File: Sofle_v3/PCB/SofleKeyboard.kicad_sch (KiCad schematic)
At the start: 97 parts, among them SW1 SW_PUSH-MX_W_LED

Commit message: design: routing and schematic beatifications
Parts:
- D1, D10, D11, D12, D13, D14, D15, D16, D17, D18, D19, D2, D20, D21, D22, D23, D24, D25, D26, D27, D28, D29, D3, D30, D4, D5, D6, D7, D8, D9: value (none) -> D; footprint (none) -> Diode_SMD:crkbd-diode
- D31, D32, D33, D34, D35, D36, D37: value (none) -> LED_sk2812_SM; footprint LED_SMD:LED_WS2812B_PLCC4_5.0x5.0mm_P3.2mm -> SofleRGB:LED_WS2812B_TwoSided; symbol SofleKeyboard:LED_sk2812_SM -> SofleKeyboard:LED_ws2812_SM
- J1: value (none) -> LED; footprint (none) -> SofleKeyboard-footprint:LED
- J2: value (none) -> 4PIN; footprint (none) -> SofleRGB:WM2211210044
- J3: value (none) -> OLED; footprint (none) -> SofleKeyboard-footprint:OLED_4Pin
- J4: value (none) -> key leds; footprint (none) -> Connector:3x1header
- J5: value (none) -> backlight sel; footprint (none) -> Connector:3x1header
- J6: value (none) -> indicator bypass; footprint (none) -> Connector:3x1header
- JP1, JP2, JP3, JP4, JP5, JP6, JP7, JP8: value (none) -> Jumper_NO_Small; footprint (none) -> SofleKeyboard-footprint:Jumper
- P1, P2: value (none) -> i2c_pin; footprint (none) -> SofleKeyboard-footprint:1pin_conn
- R1, R2: value (none) -> R; footprint (none) -> SofleKeyboard-footprint:RESISTOR_mini
- RSW1: value (none) -> SW_RST; footprint (none) -> SofleRGB:TPS635-1B43D
- SW10, SW11, SW12, SW13, SW14, SW15, SW16, SW17, SW18, SW19, SW2, SW20, SW21, SW22, SW23, SW24, SW26, SW27, SW28, SW29, SW3, SW30, SW4, SW5, SW6, SW7, SW8, SW9: value (none) -> SW_PUSH-MX_W_LED
- SW25: value (none) -> Rotary_Encoder_Switch; footprint (none) -> SofleKeyboard-footprint:RotaryEncoder_Alps_EC11E-Switch_Vertical_H20mm-keebio_modified
- U1: value (none) -> ProMicro; footprint (none) -> SofleKeyboard-footprint:ProMicro
- W1: value (none) -> jumper; footprint (none) -> SofleKeyboard-footprint:jumper_data
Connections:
- net GND: now also D31.3 (VSS), D32.3 (VSS), D33.3 (VSS), D34.3 (VSS), D35.3 (VSS), D36.3 (VSS), D37.4 (DIN); no longer D31.2 (VSS), D32.2 (VSS), D33.2 (VSS), D34.2 (VSS), D35.2 (VSS), D36.2 (VSS), D37.2 (VSS)
- net VCC: now also D31.1 (VDD), D32.1 (VDD), D33.1 (VDD), D34.1 (VDD), D35.1 (VDD), D36.1 (VDD), D37.2 (DOUT); no longer D31.4 (VDD), D32.4 (VDD), D33.4 (VDD), D34.4 (VDD), D35.4 (VDD), D36.4 (VDD), D37.4 (VDD)
- net backlight: now also SW30.4 (DIN); no longer SW30.2 (DIN)
- net underglow: now also D33.4 (DIN); no longer D33.3 (DIN)
- net SW26_D: now reaches D26.2 (A), SW26.5
- net SW1_D: now reaches D1.2 (A), SW1.5
- net SW2_D: now reaches D2.2 (A), SW2.5
- net SW3_D: now reaches D3.2 (A), SW3.5
- net SW4_D: now reaches D4.2 (A), SW4.5
- net SW5_D: now reaches D5.2 (A), SW5.5
- net SW6_D: now reaches D6.2 (A), SW6.5
- net SW8_D: now reaches D8.2 (A), SW8.5
- net SW9_D: now reaches D9.2 (A), SW9.5
- net SW10_D: now reaches D10.2 (A), SW10.5
- net SW11_D: now reaches D11.2 (A), SW11.5
- net SW12_D: now reaches D12.2 (A), SW12.5
- net SW7_D: now reaches D7.2 (A), SW7.5
- net SW13_D: now reaches D13.2 (A), SW13.5
- net SW14_D: now reaches D14.2 (A), SW14.5
- net SW15_D: now reaches D15.2 (A), SW15.5
- net SW16_D: now reaches D16.2 (A), SW16.5
- net SW17_D: now reaches D17.2 (A), SW17.5
- net SW18_D: now reaches D18.2 (A), SW18.5
- net SW21_D: now reaches D21.2 (A), SW21.5
- net SW22_D: now reaches D22.2 (A), SW22.5
- net SW23_D: now reaches D23.2 (A), SW23.5
- net SW24_D: now reaches D24.2 (A), SW24.5
- net SW20_D: now reaches D20.2 (A), SW20.5
- net SW19_D: now reaches D19.2 (A), SW19.5
- net SW27_D: now reaches D27.2 (A), SW27.5
- net SW28_D: now reaches D28.2 (A), SW28.5
- net SW29_D: now reaches D29.2 (A), SW29.5
- net SW30_D: now reaches D30.2 (A), SW30.5
- net at SW1.2 (DOUT): now also SW7.4 (DIN); no longer SW2.4 (DOUT)
- net at SW1.4 (DIN): now also SW2.2 (DOUT); no longer SW7.2 (DIN)
- net at SW8.4 (DIN): now also SW14.2 (DOUT); no longer SW2.2 (DIN)
- net at SW3.2 (DOUT): now also SW9.4 (DIN); no longer SW4.4 (DOUT)
- net at SW3.4 (DIN): now also SW4.2 (DOUT); no longer SW9.2 (DIN)
- net at SW10.4 (DIN): now also SW16.2 (DOUT); no longer SW4.2 (DIN)
- net at SW5.2 (DOUT): now also SW11.4 (DIN); no longer SW6.4 (DOUT)
- net at SW5.4 (DIN): now also SW6.2 (DOUT); no longer SW11.2 (DIN)
- net at SW12.4 (DIN): now also SW18.2 (DOUT); no longer SW6.2 (DIN)
- net at SW13.2 (DOUT): now also SW19.4 (DIN); no longer SW7.4 (DOUT)
- net at SW8.2 (DOUT): now also SW2.4 (DIN); no longer SW14.4 (DOUT)
- net at SW15.2 (DOUT): now also SW21.4 (DIN); no longer SW9.4 (DOUT)
- net at SW10.2 (DOUT): now also SW4.4 (DIN); no longer SW16.4 (DOUT)
- net at SW17.2 (DOUT): now also SW23.4 (DIN); no longer SW11.4 (DOUT)
- net at SW12.2 (DOUT): now also SW6.4 (DIN); no longer SW18.4 (DOUT)
- net at SW24.2 (DOUT): now also SW18.4 (DIN); no longer SW30.4 (DOUT)
- net at SW24.4 (DIN): now also SW30.2 (DOUT); no longer SW18.2 (DIN)
- net at SW17.4 (DIN): now also SW11.2 (DOUT); no longer SW23.2 (DIN)
- net at SW29.2 (DOUT): now also SW28.4 (DIN); no longer SW23.4 (DOUT)
- net at SW22.2 (DOUT): now also SW16.4 (DIN); no longer SW28.4 (DOUT)
- net at SW22.4 (DIN): now also SW28.2 (DOUT); no longer SW16.2 (DIN)
- net at SW15.4 (DIN): now also SW9.2 (DOUT); no longer SW21.2 (DIN)
- net at SW27.2 (DOUT): now also SW26.4 (DIN); no longer SW21.4 (DOUT)
- net at SW20.2 (DOUT): now also SW14.4 (DIN); no longer SW26.4 (DOUT)
- net at SW20.4 (DIN): now also SW26.2 (DOUT); no longer SW14.2 (DIN)
- net at SW13.4 (DIN): now also SW7.2 (DOUT); no longer SW19.2 (DIN)
- net at SW29.4 (DIN): now also SW23.2 (DOUT); no longer SW28.2 (DIN)
- net at SW27.4 (DIN): now also SW21.2 (DOUT); no longer SW26.2 (DIN)
- net at J5.2 (Pin_2): now also D36.2 (DOUT); no longer D36.1 (DOUT)
- net SW25A renamed col5
- new net: D31.2 (DOUT), D34.4 (DIN)
- new net: D31.4 (DIN), D32.2 (DOUT)
- new net: D32.4 (DIN), D33.2 (DOUT)
- new net: D34.2 (DOUT), D35.4 (DIN)
- new net: D35.2 (DOUT), D36.4 (DIN)
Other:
- note added: "TODO: - Underglow LED positioning (carefull with mounting holes - enough space to them) - Reset button footprint - Routing of everything :)))))))) - Encoder daughterboard Erledigt: - Headphone Jack footprint"
- note removed: "TODO: - Underglow LED positioning - Headphone Jack footprint - Reset button footprint - Routing of everything :)))))))) - Encoder daughterboard"
- moved on the sheet: D1, D10, D11, D12, D13, D14, D15, D16, D17, D18, D19, D2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

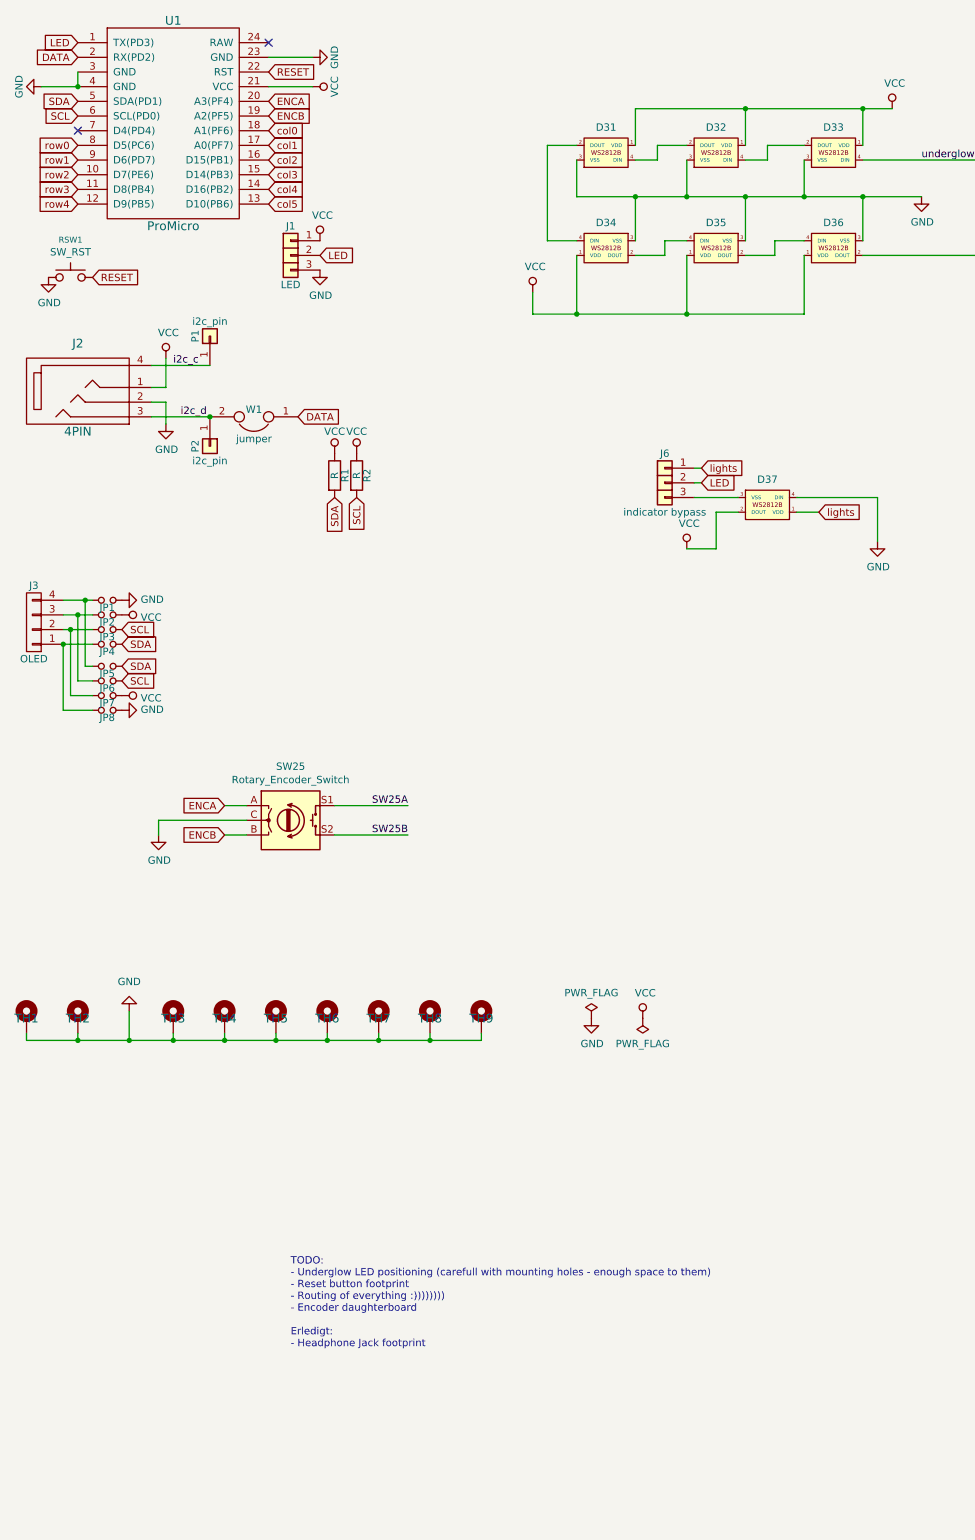
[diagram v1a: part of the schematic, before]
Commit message: design: added/changed daughterboard footprint also added jumpers for rotatry encoder side switch
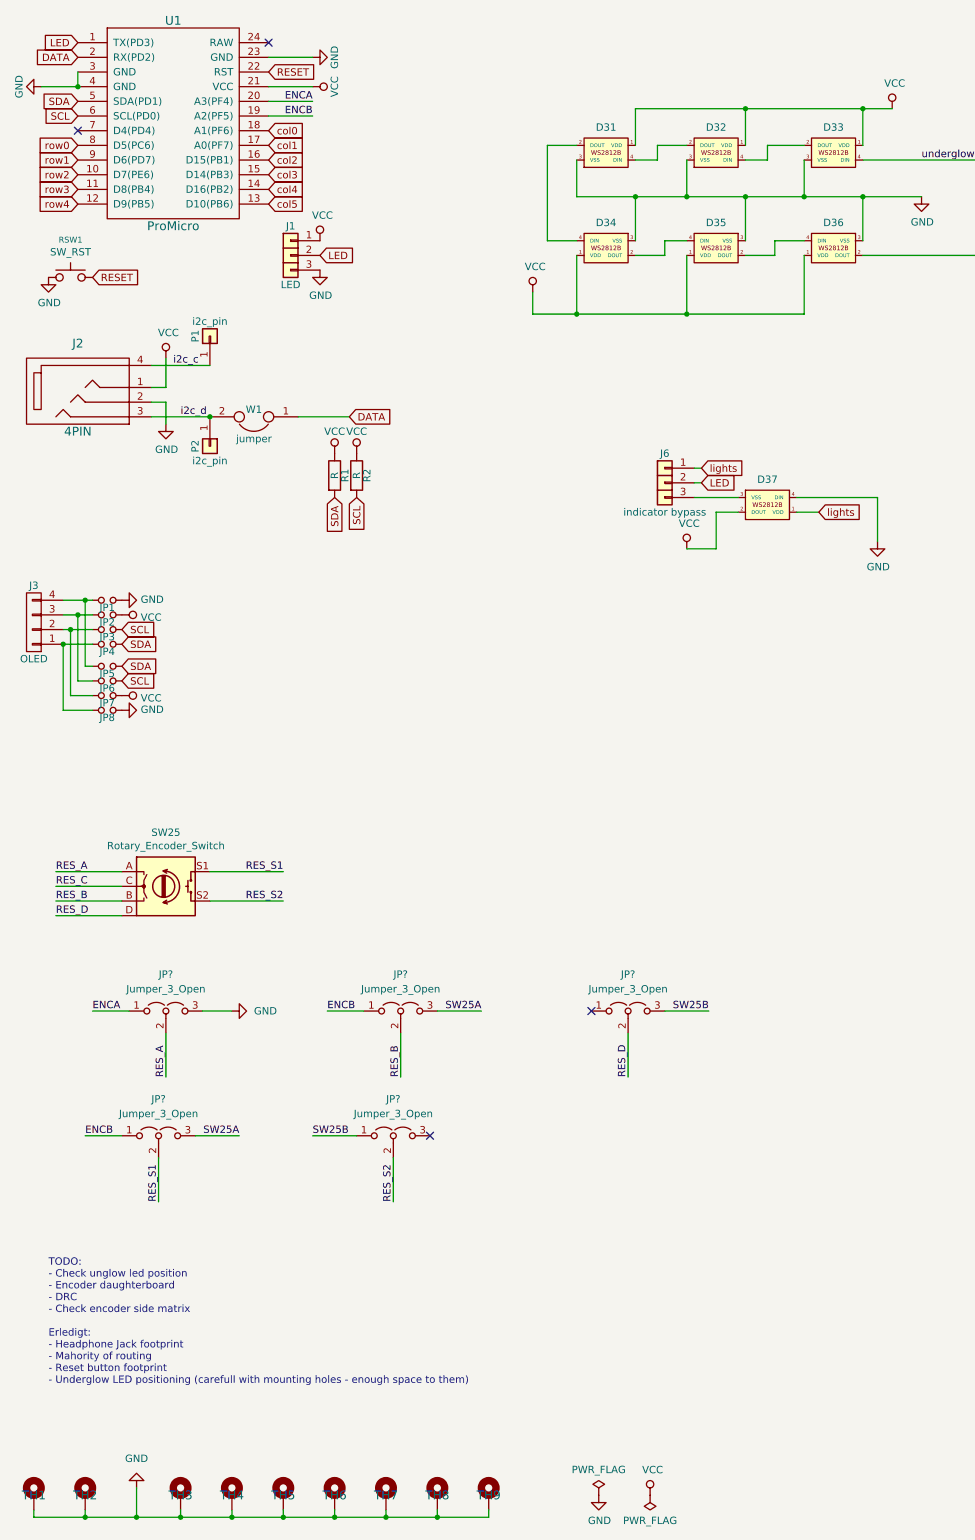
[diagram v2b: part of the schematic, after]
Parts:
- added JP? (x5): Jumper_3_Open, symbol Jumper:Jumper_3_Open
- SW25: footprint SofleKeyboard-footprint:RotaryEncoder_Alps_EC11E-Switch_Vertical_H20mm-keebio_modified -> SofleRGB:EVQWGD001_DaughterBoard; symbol SofleKeyboard-rescue:Rotary_Encoder_Switch-Device -> SofleKeyboard:RotaryEncoder_Switch4
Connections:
- net ENCA: now also JP?.1 (A); no longer SW25.A
- net ENCB: now also JP?.1 (A), JP?.1 (A); no longer SW25.B
- net GND: now also JP?.3 (B); no longer SW25.C
- net SW25B: now also JP?.1 (A), JP?.3 (B); no longer SW25.S2
- net col5: now also JP?.3 (B), JP?.3 (B); no longer SW25.S1
- new net RES_A: JP?.2 (C), SW25.A
- new net RES_B: JP?.2 (C), SW25.B
- new net RES_C: SW25.C
- new net RES_D: JP?.2 (C), SW25.D
- new net RES_S1: JP?.2 (C), SW25.S1
- new net RES_S2: JP?.2 (C), SW25.S2
- no-connect marks 4 -> 6
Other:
- note added: "TODO: - Check unglow led position - Encoder daughterboard - DRC - Check encoder side matrix Erledigt: - Headphone Jack footprint - Mahority of routing - Reset button footprint - Underglow LED positioning (carefull with mounting holes - enough space to them)"
- note removed: "TODO: - Underglow LED positioning (carefull with mounting holes - enough space to them) - Reset button footprint - Routing of everything :)))))))) - Encoder daughterboard Erledigt: - Headphone Jack footprint"
- moved on the sheet: TH1, TH2, TH3, TH4, TH5, TH6, TH7, TH8, TH9

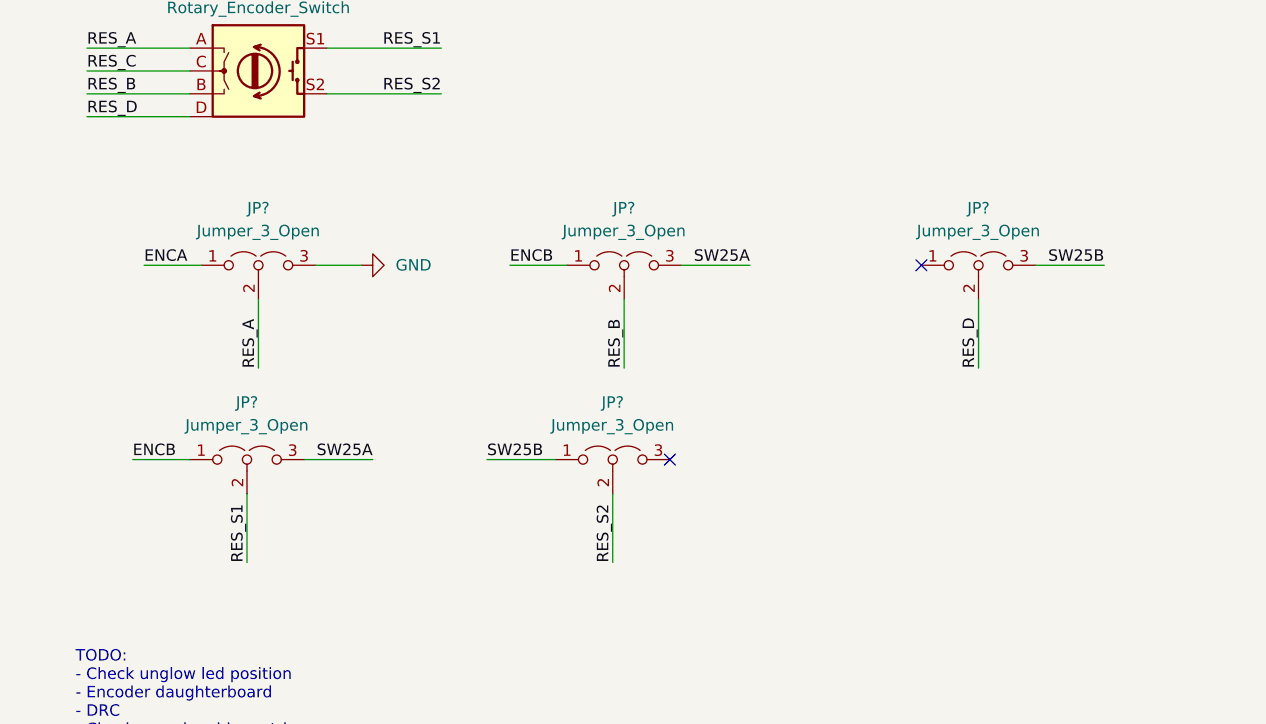
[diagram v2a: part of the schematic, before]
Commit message: design: minor orientation change added daughterboard first drc checks
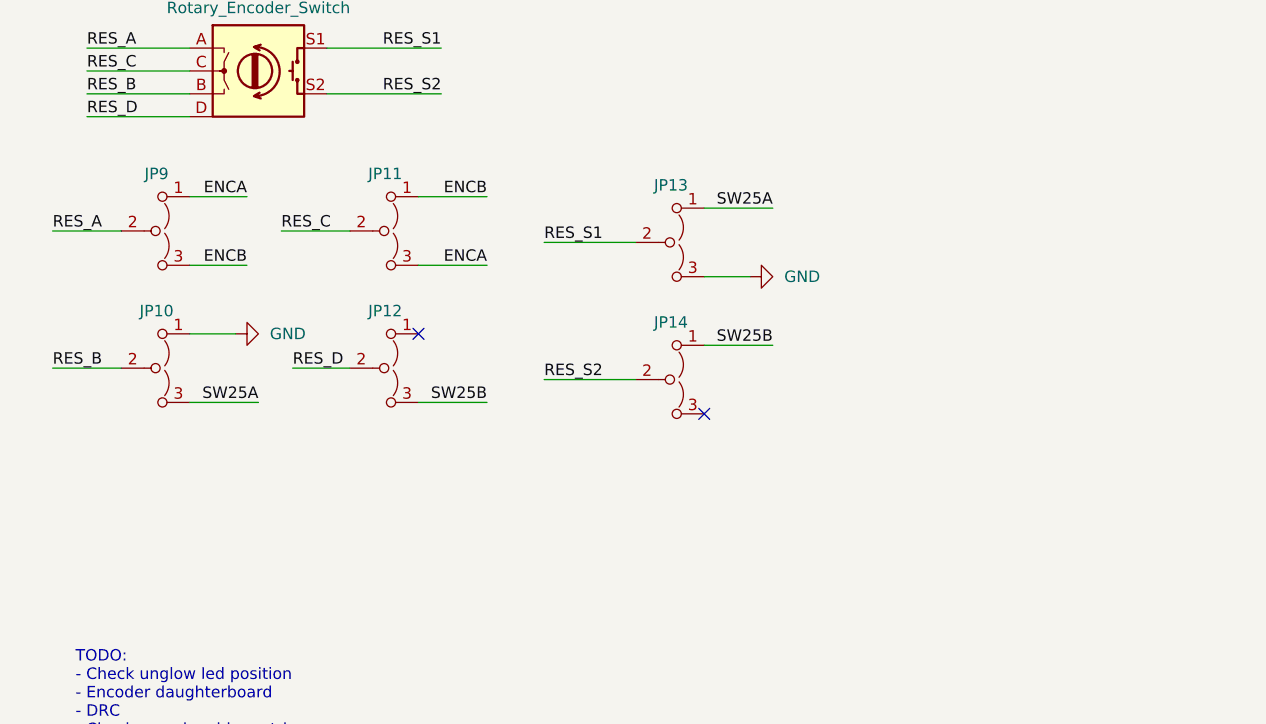
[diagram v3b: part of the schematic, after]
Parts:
- removed JP? (x5): Jumper_3_Open, symbol Jumper:Jumper_3_Open
- added JP10, JP11, JP12, JP13, JP14, JP9: Jumper_3_Open_Custom, SofleRGB:CustomJumper, symbol SofleKeyboard:Jumper_3_Open_Custom
- W1: footprint SofleKeyboard-footprint:jumper_data -> Jumper:SolderJumper-2_P1.3mm_Bridged_RoundedPad1.0x1.5mm
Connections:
- net ENCA: now also JP11.3 (B), JP9.1 (A)
- net ENCB: now also JP11.1 (A), JP9.3 (B)
- net GND: now also JP10.1 (A), JP13.3 (B)
- net RES_A: now also JP9.2 (C)
- net RES_B: now also JP10.2 (C)
- net RES_C: now also JP11.2 (C)
- net RES_D: now also JP12.2 (C)
- net RES_S1: now also JP13.2 (C)
- net RES_S2: now also JP14.2 (C)
- net SW25B: now also JP12.3 (B), JP14.1 (A)
- net col5: now also JP10.3 (B), JP13.1 (A)

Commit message: design rotated outer thumb key
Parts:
- J1: footprint SofleKeyboard-footprint:LED -> SofleRGB:LED
- SW1, SW10, SW11, SW12, SW13, SW14, SW15, SW16, SW17, SW18, SW19, SW2, SW20, SW21, SW22, SW23, SW24, SW26, SW27, SW28, SW29, SW3, SW30, SW4, SW5, SW6, SW7, SW8, SW9: footprint Button_Switch_Keyboard:SK6812MINI_and_cherry -> SofleRGB:5050_and_cherry
